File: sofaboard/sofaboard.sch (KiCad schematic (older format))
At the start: 164 parts

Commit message: Adds microcontroller
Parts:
- added C?: 1uF, symbol Device:CP
- added C? (x2): 10pF, symbol Device:C
- added C?: 0.1uF, symbol Device:CP
- added J?: USB_B_Micro, symbol Connector:USB_B_Micro
- added R? (x2): 22, symbol Device:R
- added R?: 1K, symbol Device:R
- added SW?: SW_Push, symbol Switch:SW_Push
- added U?: AT90USB1286-AU, Package_QFP:TQFP-64_14x14mm_P0.8mm, symbol MCU_Microchip_AVR:AT90USB1286-AU
- added Y?: 16MHz, symbol Device:Crystal
- gave numbers to parts that had none: 164
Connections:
- net col0: now also U?.17 (PB7)
- net col1: now also U?.25 (PD0)
- net col10: now also U?.34 (PE1)
- net col11: now also U?.35 (PC0)
- net col12: now also U?.36 (PC1)
- net col13: now also U?.37 (PC2)
- net col14: now also U?.38 (PC3)
- net col2: now also U?.26 (PD1)
- net col3: now also U?.27 (PD2)
- net col4: now also U?.28 (PD3)
- net col5: now also U?.29 (PD4)
- net col6: now also U?.30 (PD5)
- net col7: now also U?.39 (PC4)
- net col8: now also U?.32 (PD7)
- net col9: now also U?.33 (PE0)
- net row0: now also U?.16 (PB6)
- net row1: now also U?.15 (PB5)
- net row2: now also U?.14 (PB4)
- net row3: now also U?.13 (PB3)
- net row4: now also U?.12 (PB2)
- net row5: now also U?.11 (PB1)
- new net: SW?.2, U?.20 (~RESET)
- new net: C?.2, U?.23 (XTAL2), Y?.2
- new net: C?.2, U?.24 (XTAL1), Y?.1
- new net: R?.1, U?.4 (D-)
- new net: R?.1, U?.43 (PE2/~HWB)
- new net: R?.1, U?.5 (D+)
- new net: C?.2, U?.62 (AREF)
- new net: C?.1, U?.7 (UCAP)
- new net: J?.2 (D-), R?.2
- new net: J?.3 (D+), R?.2
- new net +5V: J?.1 (VBUS), U?.21 (VCC), U?.3 (UVCC), U?.52 (VCC), U?.64 (AVCC), U?.8 (VBUS)
- new net GND: C?.1, C?.1, C?.1, C?.2, J?.5 (GND), J?.6 (Shield), R?.2, SW?.1, U?.22 (GND), U?.53 (GND), U?.6 (UGND), U?.63 (GND)
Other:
- moved on the sheet: D1, D10, D11, D12, D13, D14, D15, D16, D17, D18, D19, D2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

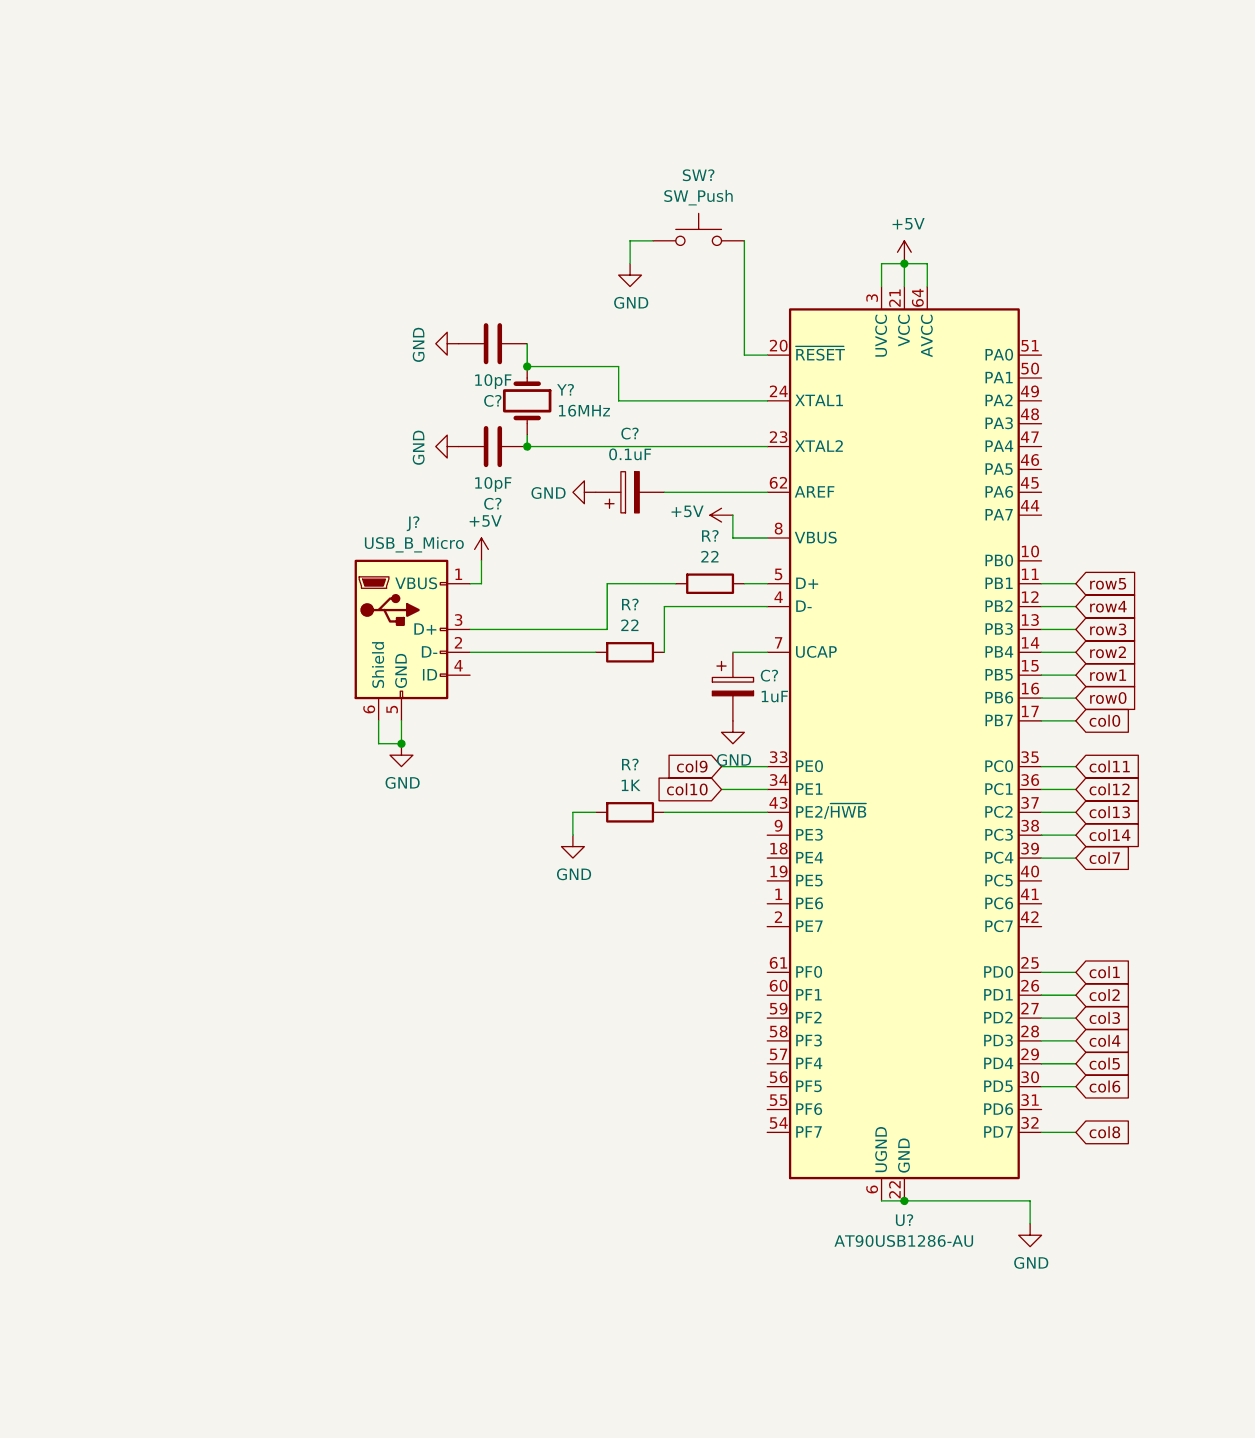
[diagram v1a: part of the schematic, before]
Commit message: Fixes schematic layout
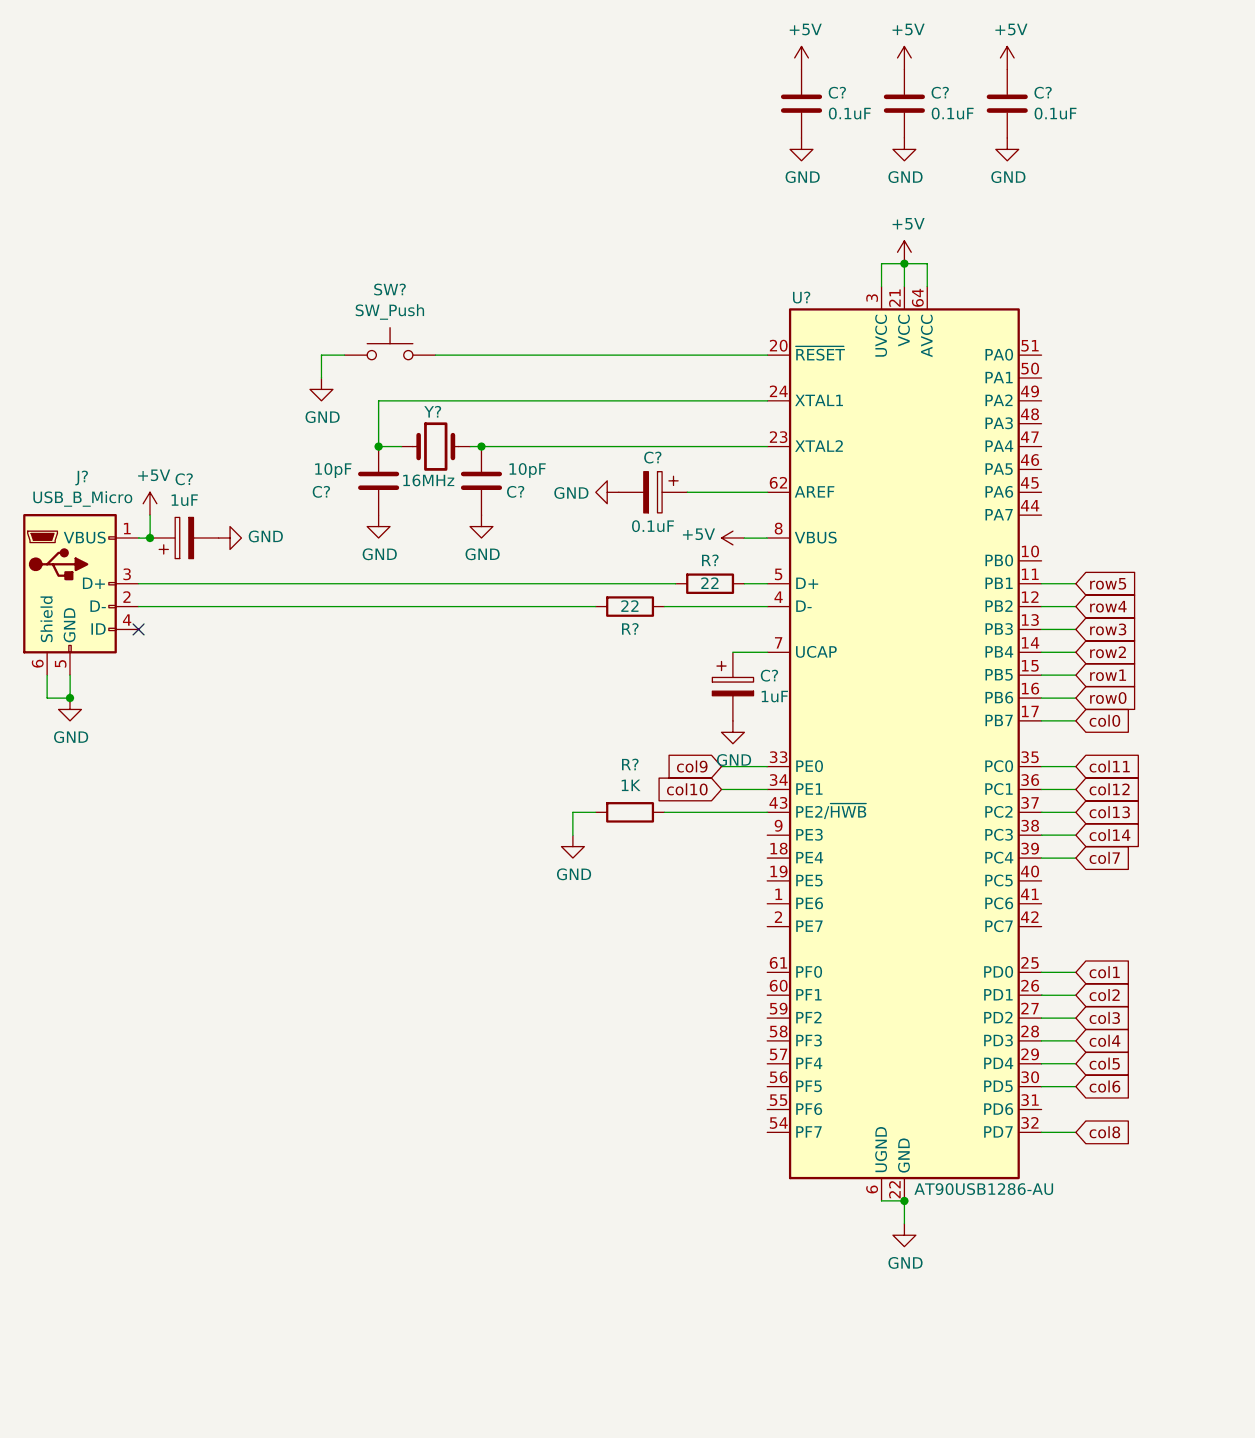
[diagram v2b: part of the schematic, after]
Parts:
- added C?: 1uF, symbol Device:CP
- added C? (x3): 0.1uF, symbol Device:C
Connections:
- net +5V: now also C?.1, C?.1, C?.1, C?.1
- net GND: now also C?.2, C?.2, C?.2, C?.2, C?.2; no longer C?.1
- net at U?.62 (AREF): now also C?.1; no longer C?.2
- no-connect marks 0 -> 1
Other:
- moved on the sheet: C?, J?, R?, SW?, Y?

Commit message: Fixes annotations and no connection labels
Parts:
- gave numbers to parts that had none: 15
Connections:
- no-connect marks 1 -> 27
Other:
- moved on the sheet: C1, C2, C3, C4, C5, C6, C7, C8, D1, D10, D11, D12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

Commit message: Assigns footprints
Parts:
- C1, C2, C3, C4, C5, C6, C7, C8: footprint (none) -> Capacitor_SMD:C_0805_2012Metric_Pad1.15x1.40mm_HandSolder
- D1, D10, D11, D12, D13, D14, D15, D16, D17, D18, D19, D2, D20, D21, D22, D23, D24, D25, D26, D27, D28, D29, D3, D30, D31, D32, D33, D34, D35, D36, D37, D38, D39, D4, D40, D41, D42, D43, D44, D45, D46, D47, D48, D49, D5, D50, D51, D52, D53, D54, D55, D56, D57, D58, D59, D6, D60, D61, D62, D63, D64, D65, D66, D67, D68, D69, D7, D70, D71, D72, D73, D74, D75, D76, D77, D78, D79, D8, D80, D81, D82, D9: footprint (none) -> Diode_SMD:D_MELF_Handsoldering
- J1: footprint (none) -> Connector_USB:USB_Micro-B_Amphenol_10103594-0001LF_Horizontal
- R1, R2, R3: footprint (none) -> Resistor_SMD:R_0805_2012Metric_Pad1.15x1.40mm_HandSolder
- SW1, SW10, SW11, SW12, SW13, SW14, SW15, SW16, SW17, SW18, SW19, SW2, SW20, SW21, SW22, SW23, SW24, SW25, SW26, SW27, SW28, SW29, SW3, SW30, SW31, SW32, SW33, SW34, SW35, SW36, SW37, SW38, SW39, SW4, SW40, SW41, SW42, SW43, SW44, SW45, SW46, SW47, SW48, SW49, SW5, SW50, SW51, SW52, SW53, SW54, SW55, SW56, SW57, SW58, SW59, SW6, SW60, SW61, SW62, SW63, SW64, SW65, SW66, SW67, SW68, SW69, SW7, SW70, SW71, SW72, SW73, SW74, SW75, SW76, SW77, SW78, SW79, SW8, SW80, SW81, SW82, SW9: footprint (none) -> Button_Switch_Keyboard:SW_Cherry_MX1A_1.00u_Plate
- SW83: footprint (none) -> Button_Switch_THT:SW_PUSH_6mm_H5mm
- Y1: footprint (none) -> Crystal:Crystal_SMD_HC49-SD_HandSoldering

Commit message: Switch Placement
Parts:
- SW1, SW10, SW11, SW12, SW13, SW14, SW15, SW16, SW17, SW18, SW19, SW2, SW20, SW21, SW22, SW23, SW24, SW25, SW26, SW27, SW28, SW29, SW3, SW30, SW31, SW32, SW33, SW34, SW35, SW36, SW37, SW38, SW39, SW4, SW40, SW41, SW42, SW43, SW44, SW45, SW46, SW47, SW48, SW49, SW5, SW50, SW51, SW52, SW53, SW54, SW55, SW56, SW57, SW58, SW59, SW6, SW60, SW61, SW62, SW63, SW64, SW65, SW66, SW67, SW68, SW69, SW7, SW70, SW71, SW72, SW73, SW74, SW75, SW76, SW77, SW78, SW79, SW8, SW80, SW81, SW82, SW9: footprint Button_Switch_Keyboard:SW_Cherry_MX1A_1.00u_Plate -> Cherry:SW_Cherry_MX1A_1.00u_Plate_clean

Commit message: Change crystal footprint
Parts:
- Y1: footprint Crystal:Crystal_SMD_HC49-SD_HandSoldering -> Cherry:16MHz Crystal
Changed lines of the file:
@@
 F 0 "Y1" H 3300 3450 50  0000 L CNN
 F 1 "16MHz" H 3200 3150 50  0000 L CNN
-F 2 "Crystal:Crystal_SMD_HC49-SD_HandSoldering" H 3350 3300 50  0001 C CNN
+F 2 "Cherry:16MHz Crystal" H 3350 3300 50  0001 C CNN
 F 3 "~" H 3350 3300 50  0001 C CNN
 	1    3350 3300

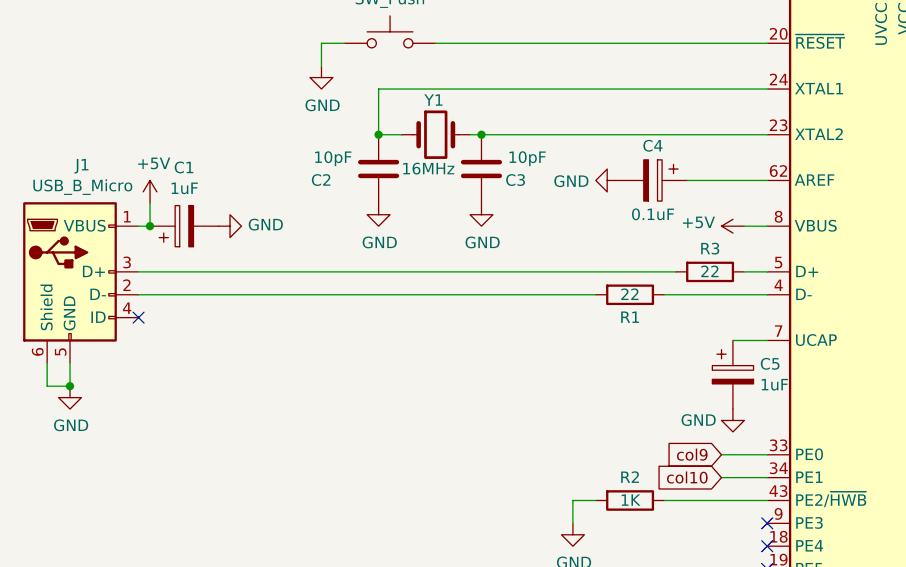
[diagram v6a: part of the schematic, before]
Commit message: Improve routing and board dimensions
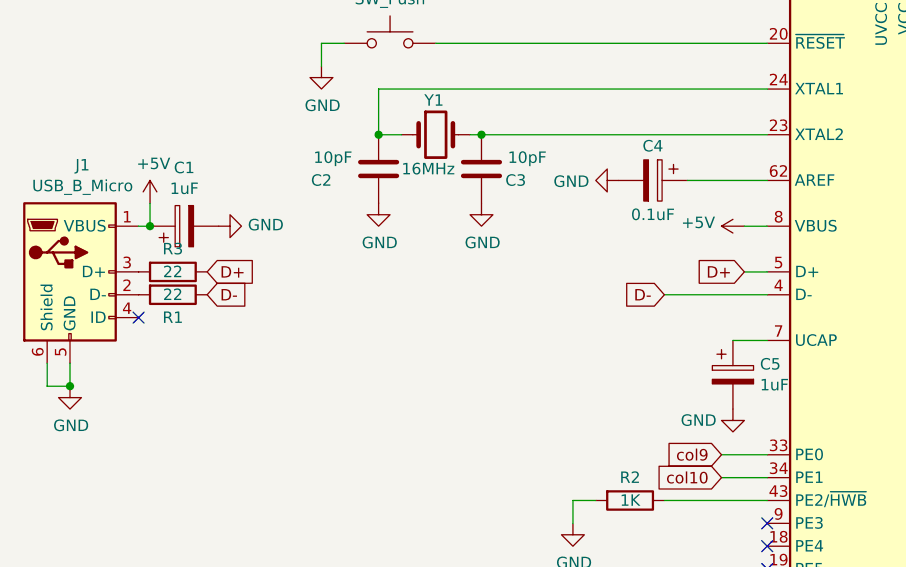
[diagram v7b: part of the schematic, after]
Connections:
- net D-: now reaches R1.1, U1.4 (D-)
- net D+: now reaches R3.1, U1.5 (D+)
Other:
- moved on the sheet: R1, R3
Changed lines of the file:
@@
 EESchema Schematic File Version 4
-EELAYER 26 0
+LIBS:sofaboard-cache
+EELAYER 29 0
 EELAYER END
 $Descr A2 23386 16535
@@
 L Device:R R3
 U 1 1 5CE1B4FE
-P 4550 3900
-F 0 "R3" V 4450 3900 50  0000 C CNN
-F 1 "22" V 4550 3900 50  0000 C CNN
-F 2 "Resistor_SMD:R_0805_2012Metric_Pad1.15x1.40mm_HandSolder" V 4480 3900 50  0001 C CNN
-F 3 "~" H 4550 3900 50  0001 C CNN
-	1    4550 3900
+P 2200 3900
+F 0 "R3" V 2100 3900 50  0000 C CNN
+F 1 "22" V 2200 3900 50  0000 C CNN
+F 2 "Resistor_SMD:R_0805_2012Metric_Pad1.15x1.40mm_HandSolder" V 2130 3900 50  0001 C CNN
+F 3 "~" H 2200 3900 50  0001 C CNN
+	1    2200 3900
 	0    1    1    0
 $EndComp
@@
 L Device:R R1
 U 1 1 5CE1D9C5
-P 4200 4000
-F 0 "R1" V 4300 4000 50  0000 C CNN
-F 1 "22" V 4200 4000 50  0000 C CNN
-F 2 "Resistor_SMD:R_0805_2012Metric_Pad1.15x1.40mm_HandSolder" V 4130 4000 50  0001 C CNN
-F 3 "~" H 4200 4000 50  0001 C CNN
-	1    4200 4000
+P 2200 4000
+F 0 "R1" V 2300 4000 50  0000 C CNN
+F 1 "22" V 2200 4000 50  0000 C CNN
+F 2 "Resistor_SMD:R_0805_2012Metric_Pad1.15x1.40mm_HandSolder" V 2130 4000 50  0001 C CNN
+F 3 "~" H 2200 4000 50  0001 C CNN
+	1    2200 4000
 	0    1    1    0
 $EndComp
@@
 	1    0    0    -1
 $EndComp
-Wire Wire Line
-	2050 4000 4050 4000
 $Comp
 L Device:C C3
@@
 	5400 6600 5400 6700
 Connection ~ 5400 6600
-Wire Wire Line
-	2050 3900 4400 3900
 NoConn ~ 2050 4100
 Wire Wire Line
@@
 NoConn ~ 6000 3000
 NoConn ~ 6000 2900
+Text GLabel 4700 3900 0    50   Input ~ 0
+D+
+Text GLabel 2350 3900 2    50   Input ~ 0
+D+
+Text GLabel 4350 4000 0    50   Input ~ 0
+D-
+Text GLabel 2350 4000 2    50   Input ~ 0
+D-
 $EndSCHEMATC
